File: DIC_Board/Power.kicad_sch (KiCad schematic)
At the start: 77 parts, among them Q100 CSD18542KTTT, Q101 CSD18542KTTT, U10 TPS552882RPMR, U11 TPSM53603RDAR, U12 TPSM53603RDAR, U13 TPSM53603RDAR, U14 TPSM53603RDAR

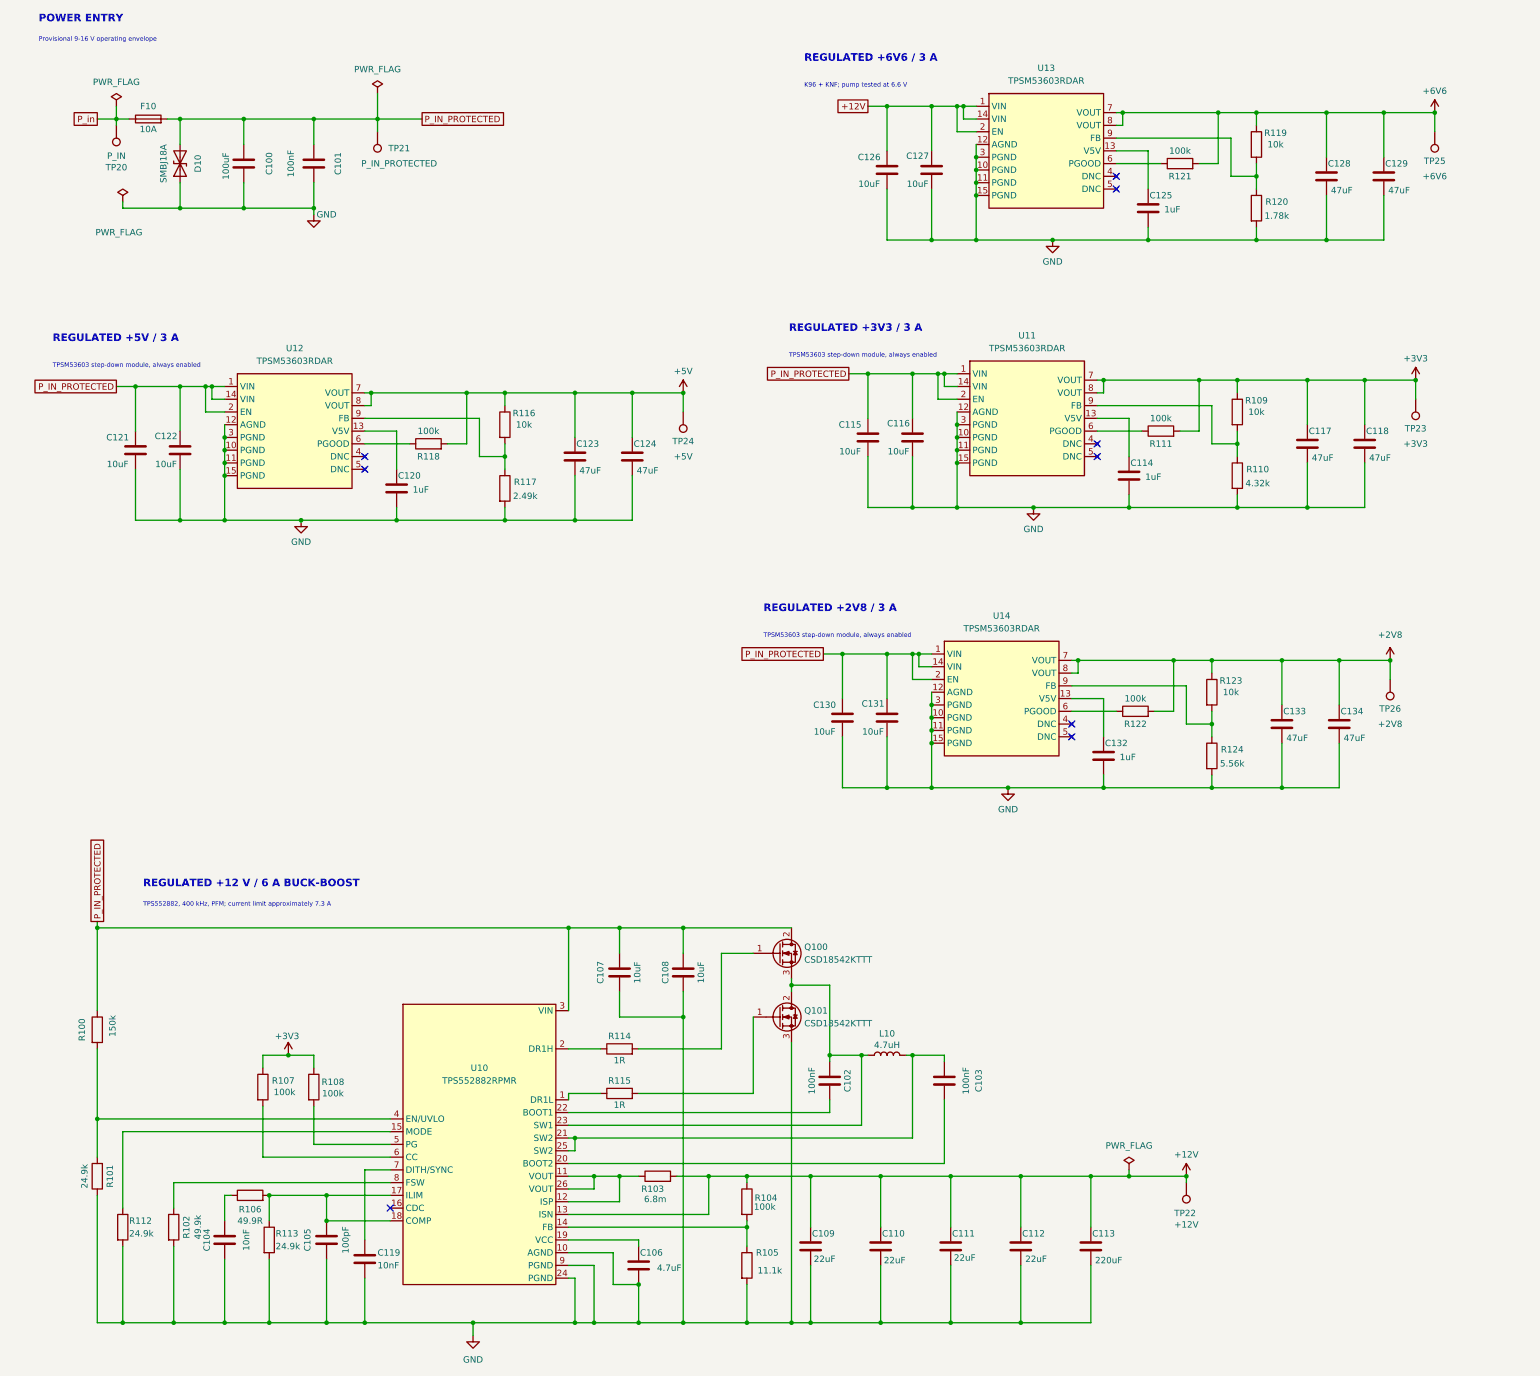
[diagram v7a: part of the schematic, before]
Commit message: Separated the power sheets, did the sensor sheets.
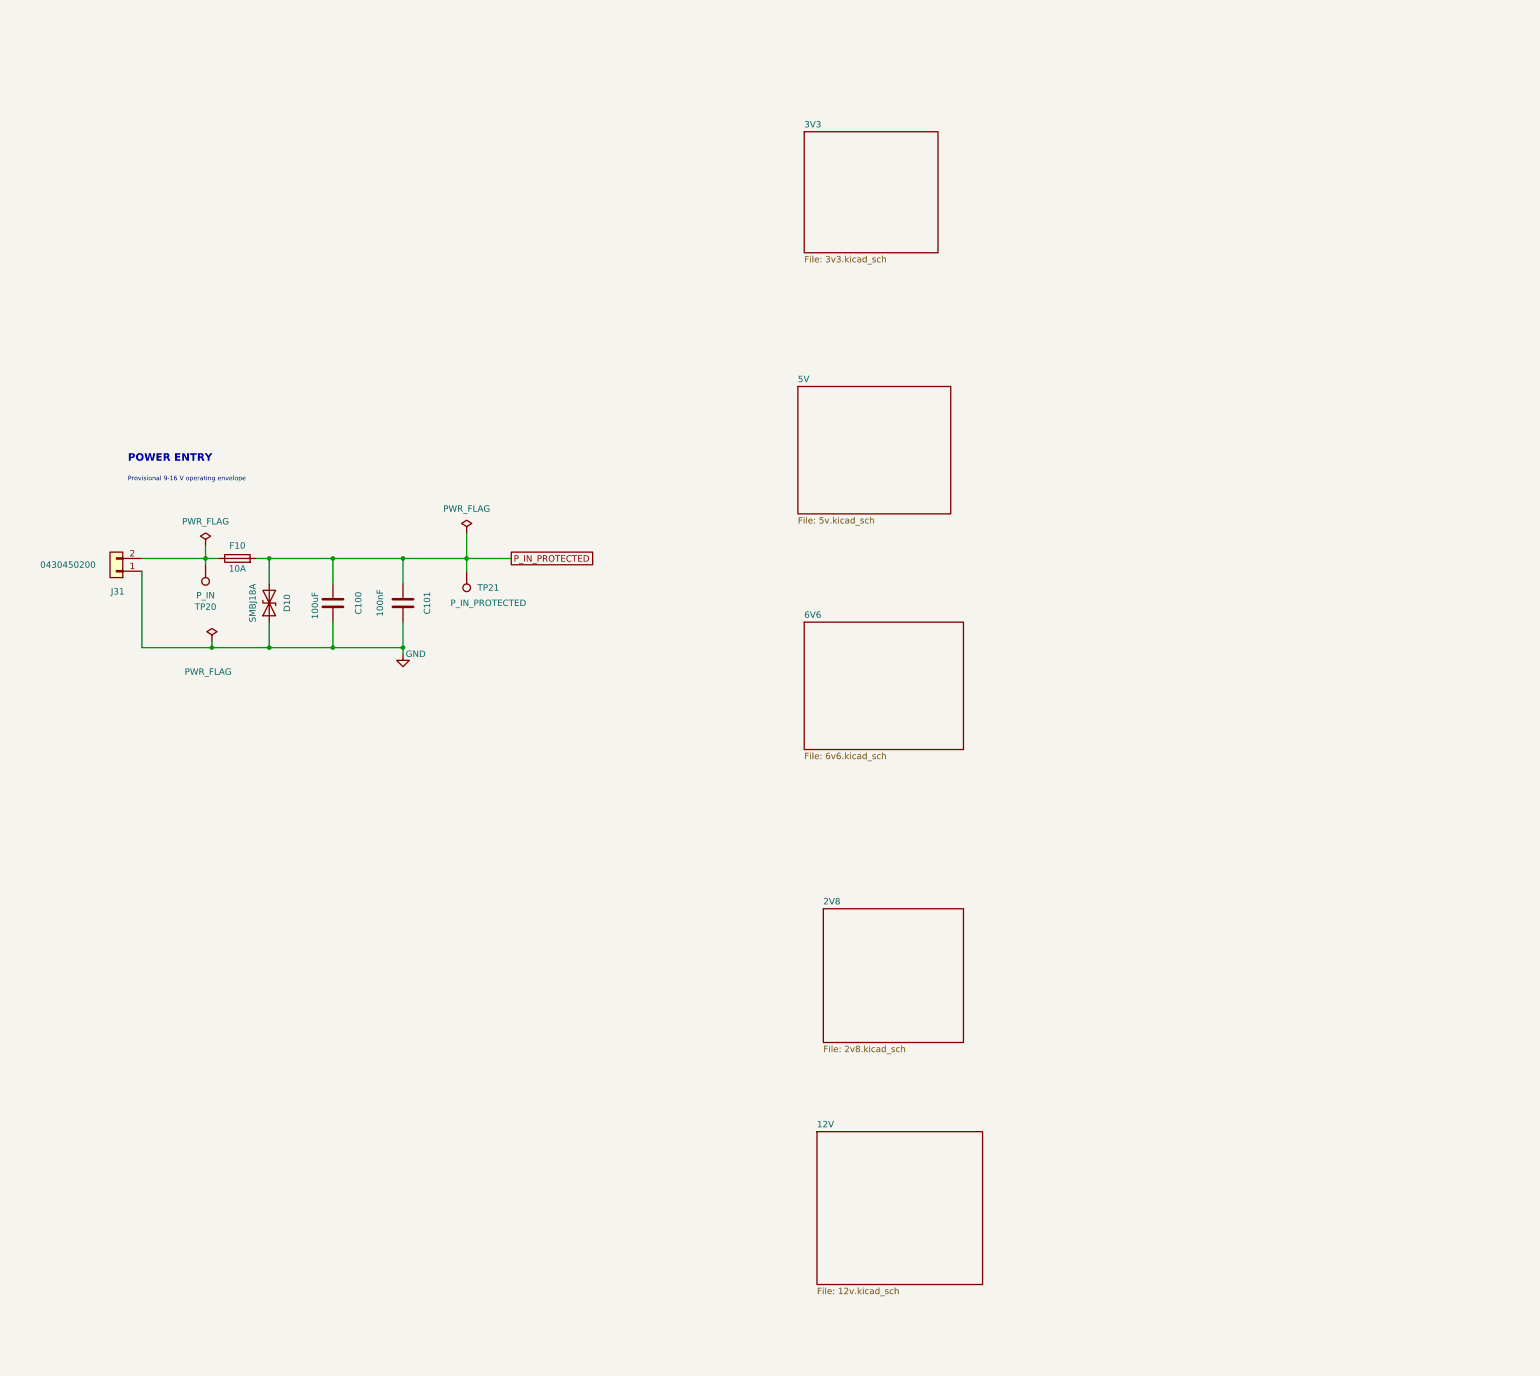
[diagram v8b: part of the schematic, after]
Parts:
- removed C102, C103: 100nF, Capacitor_SMD:C_0402_1005Metric, symbol Device:C
- removed C104, C119: 10nF, Capacitor_SMD:C_0402_1005Metric, symbol Device:C
- removed C105: 100pF, Capacitor_SMD:C_0402_1005Metric, symbol Device:C
- removed C106: 4.7uF, Capacitor_SMD:C_0603_1608Metric, symbol Device:C
- removed C107, C108, C115, C116, C121, C122, C126, C127, C130, C131: 10uF, Capacitor_SMD:C_1206_3216Metric, symbol Device:C
- removed C109, C110, C111, C112: 22uF, Capacitor_SMD:C_1210_3225Metric, symbol Device:C
- removed C113: 220uF, Capacitor_SMD:CP_Elec_8x10.5, symbol Device:C
- removed C114, C120, C125, C132: 1uF, Capacitor_SMD:C_0603_1608Metric, symbol Device:C
- removed C117, C118, C123, C124, C128, C129, C133, C134: 47uF, Capacitor_SMD:C_1210_3225Metric, symbol Device:C
- removed L10: 4.7uH, Inductor_SMD:L_Coilcraft_XAL1010-XXX, symbol Device:L
- removed Q100, Q101: CSD18542KTTT, Package_TO_SOT_SMD:TO-263-3_TabPin2, symbol Transistor_FET:Q_NMOS_GDS
- removed R100: 150k, Resistor_SMD:R_0402_1005Metric, symbol Device:R
- removed R101, R112, R113: 24.9k, Resistor_SMD:R_0402_1005Metric, symbol Device:R
- removed R102: 49.9k, Resistor_SMD:R_0402_1005Metric, symbol Device:R
- removed R103: 6.8m, Resistor_SMD:R_2512_6332Metric, symbol Device:R
- removed R104, R107, R108, R111, R118, R121, R122: 100k, Resistor_SMD:R_0402_1005Metric, symbol Device:R
- removed R105: 11.1k, Resistor_SMD:R_0402_1005Metric, symbol Device:R
- removed R106: 49.9R, Resistor_SMD:R_0402_1005Metric, symbol Device:R
- removed R109, R116, R119, R123: 10k, Resistor_SMD:R_0402_1005Metric, symbol Device:R
- removed R110: 4.32k, Resistor_SMD:R_0402_1005Metric, symbol Device:R
- removed R114, R115: 1R, Resistor_SMD:R_0603_1608Metric, symbol Device:R
- removed R117: 2.49k, Resistor_SMD:R_0402_1005Metric, symbol Device:R
- removed R120: 1.78k, Resistor_SMD:R_0402_1005Metric, symbol Device:R
- removed R124: 5.56k, Resistor_SMD:R_0402_1005Metric, symbol Device:R
- removed TP22: +12V, TestPoint:TestPoint_Plated_Hole_D2.0mm, symbol Connector:TestPoint
- removed TP23: +3V3, TestPoint:TestPoint_Plated_Hole_D2.0mm, symbol Connector:TestPoint
- removed TP24: +5V, TestPoint:TestPoint_Plated_Hole_D2.0mm, symbol Connector:TestPoint
- removed TP25: +6V6, TestPoint:TestPoint_Plated_Hole_D2.0mm, symbol Connector:TestPoint
- removed TP26: +2V8, TestPoint:TestPoint_Plated_Hole_D2.0mm, symbol Connector:TestPoint
- removed U10: TPS552882RPMR, symbol DIC_Board:TPS552882
- removed U11, U12, U13, U14: TPSM53603RDAR, Package_DFN_QFN:Texas_B3QFN-14-1EP_5x5.5mm_P0.65mm_ThermalVia, symbol DIC_Board:TPSM53603RDA
- added J31: 0430450200, Connector_Molex:Molex_Micro-Fit_3.0_43045-0200_2x01_P3.00mm_Horizontal, symbol Connector_Generic:Conn_01x02
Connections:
- net GND: now also J31.1 (Pin_1)
- net P_in: no longer names the net of F10.1, TP20.1
- net P_in: now also J31.2 (Pin_2)
- no-connect marks 9 -> 0
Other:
- added sheet 12V (12v.kicad_sch)
- added sheet 2V8 (2v8.kicad_sch)
- added sheet 3V3 (3v3.kicad_sch)
- added sheet 5V (5v.kicad_sch)
- added sheet 6V6 (6v6.kicad_sch)
- note removed: "K96 + KNF; pump tested at 6.6 V"
- note removed: "REGULATED +12 V / 6 A BUCK-BOOST"
- note removed: "REGULATED +2V8 / 3 A"
- note removed: "REGULATED +3V3 / 3 A"
- note removed: "REGULATED +5V / 3 A"
- note removed: "REGULATED +6V6 / 3 A"
- note removed: "TPS552882, 400 kHz, PFM; current limit approximately 7.3 A"
- note removed: "TPSM53603 step-down module, always enabled"
- moved on the sheet: C100, C101, D10, F10, TP20, TP21
